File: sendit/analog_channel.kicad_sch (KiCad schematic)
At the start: 6 parts

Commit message: bigger update
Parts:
- added C5: 100nF, Capacitor_SMD:C_0805_2012Metric_Pad1.18x1.45mm_HandSolder, symbol Device:C_Small
- added F1: 30v / 30mA, Fuse:Fuse_0603_1608Metric, symbol Device:Polyfuse_Small
- added R13: 1.5K 0.1%, Resistor_SMD:R_1206_3216Metric_Pad1.30x1.75mm_HandSolder, symbol Device:R_Small_US
- added R16: 910 0.1%, Resistor_SMD:R_1206_3216Metric_Pad1.30x1.75mm_HandSolder, symbol Device:R_Small_US
- added R2: 470 0.1%, Resistor_SMD:R_1206_3216Metric_Pad1.30x1.75mm_HandSolder, symbol Device:R_Small_US
- added R20: 1k 0.1%, Resistor_SMD:R_1206_3216Metric_Pad1.30x1.75mm_HandSolder, symbol Device:R_Small_US
- added R70: 165 0.1%, Resistor_SMD:R_1206_3216Metric_Pad1.30x1.75mm_HandSolder, symbol Device:R_Small_US
- added R8: 13K 0.1%, Resistor_SMD:R_1206_3216Metric_Pad1.30x1.75mm_HandSolder, symbol Device:R_Small_US
- added TP1, TP9: TestPoint, TestPoint:TestPoint_Pad_D1.0mm, symbol Connector:TestPoint
- added TP81: TestPoint, symbol Connector:TestPoint
- added U3: TMUX4052PWR, yarrboard:TSSOP16-PW_TEX, symbol yarrboard:TMUX4052PWR
- renumbered C11 to C1, D4 to D1, INPUT4 to INPUT1, J4 to J1, R19 to R1
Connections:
- net +24V: now also C5.1, U3.16 (VDD)
- net +3.3V: now also R20.2
- net A0: now also U3.10 (A0)
- net A1: now also U3.9 (A1)
- net EN: now also U3.6 (*EN)
- net GND: now also C5.2, R13.1, R16.1, R70.1, U3.7 (VSS), U3.8 (GND)
- net OUTPUT: now also TP81.1
- net at J1.1 (Pin_1), J1.3 (Pin_3), J1.5 (Pin_5): now also F1.1; no longer INPUT1.1 (Pin_1)
- net ADC MUX - TMUX4052/DA: no longer names the net of D9.3 (COM), INPUT1.2 (Pin_2)
- net ADC MUX - TMUX4052/DA: now also TP1.1, U3.13 (DA)
- net ADC MUX - TMUX4052/DB: no longer names the net of R1.1
- net ADC MUX - TMUX4052/DB: now also TP9.1, U3.3 (DB)
- new net: R20.1, U3.15 (S2A), U3.2 (S2B)
- new net: F1.2, INPUT1.1 (Pin_1)
- new net: R13.2, R8.1, U3.5 (S1B)
- new net: R16.2, R2.1, U3.4 (S3B)
- new net: R8.2, U3.14 (S1A)
- new net: R70.2, U3.1 (S0B), U3.12 (S0A)
- new net: R2.2, U3.11 (S3A)
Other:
- removed sheet 0-1000 ohm
- removed sheet 0-32v
- removed sheet 0-5v
- removed sheet 4-20mA
- removed sheet ADC MUX - TMUX4052
- note added: "(resistor wired from input to ground)"
- note added: "0-1000 ohm Resistance Sensor"
- note added: "32v to 3.3v Voltage Divider"
- note added: "4-20ma Current Sensor"
- note added: "5v to 3.3v Voltage Divider"
- note added: "Analog MUX - 4:1 - 2CH"
- note added: "Different Types of Input Signals:"
- note added: "Input Stage"
- note added: "Output Stage"
- moved on the sheet: C1, D1, D9, INPUT1, J1, R1

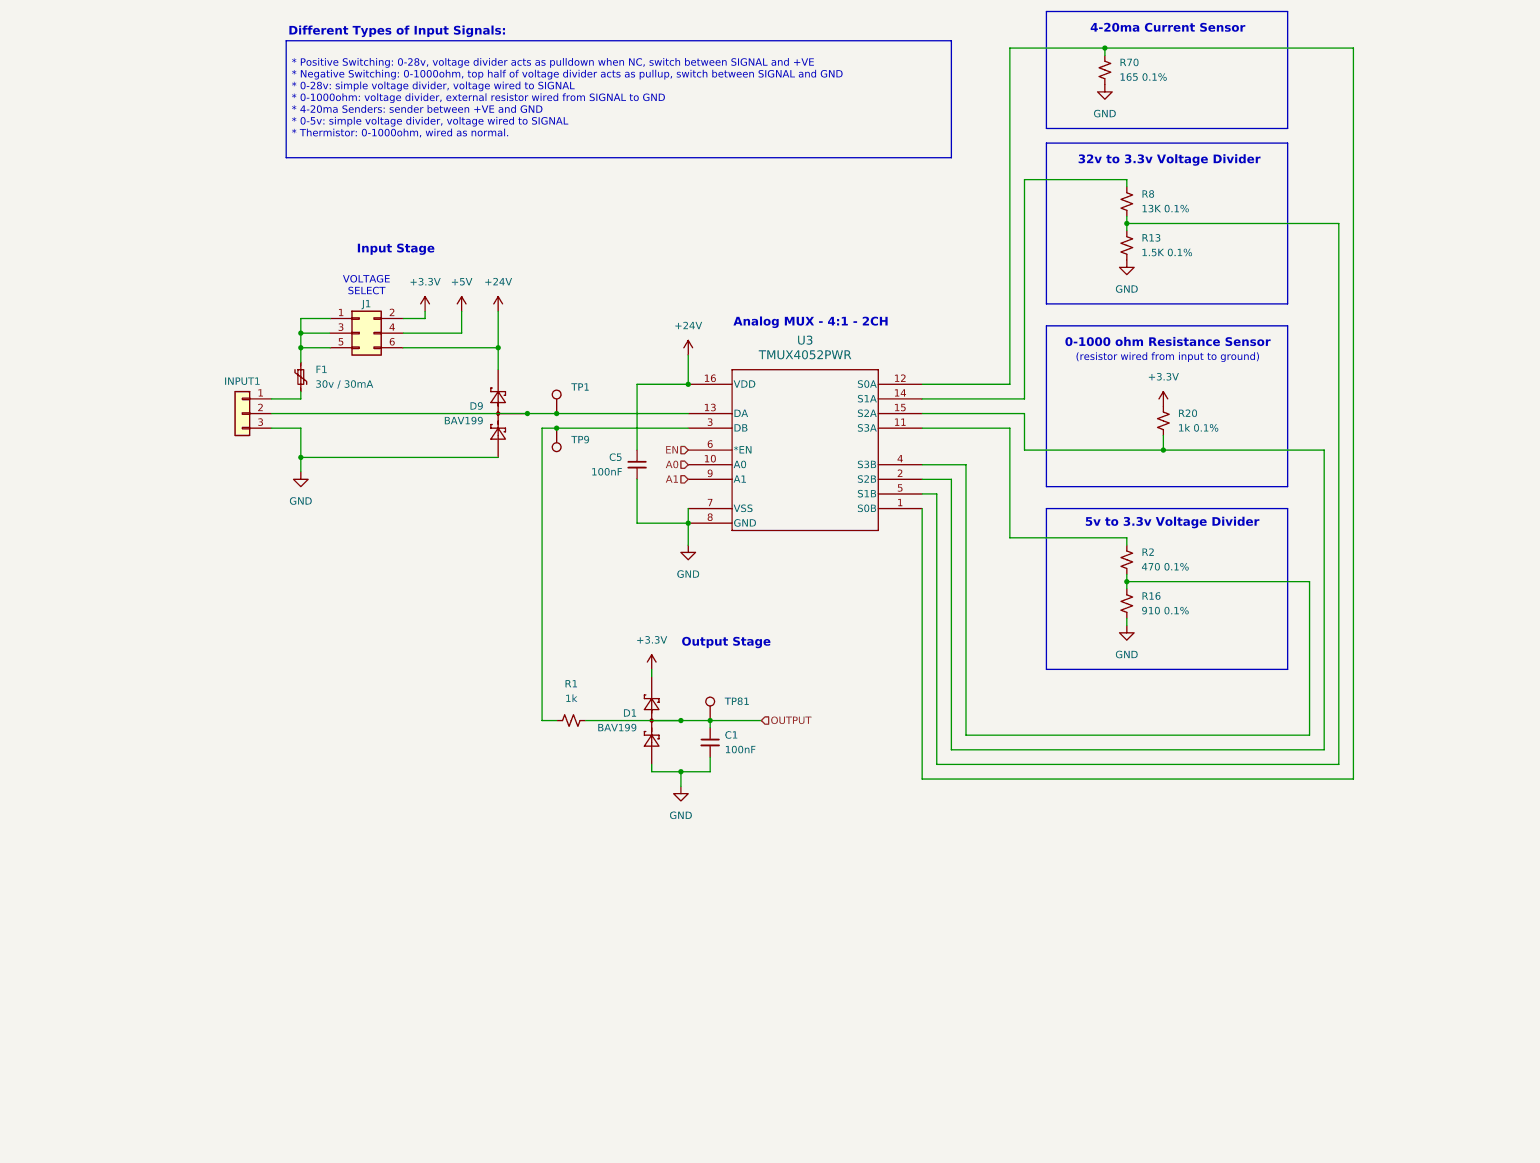
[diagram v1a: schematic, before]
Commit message: changed from mux to pin jumpers
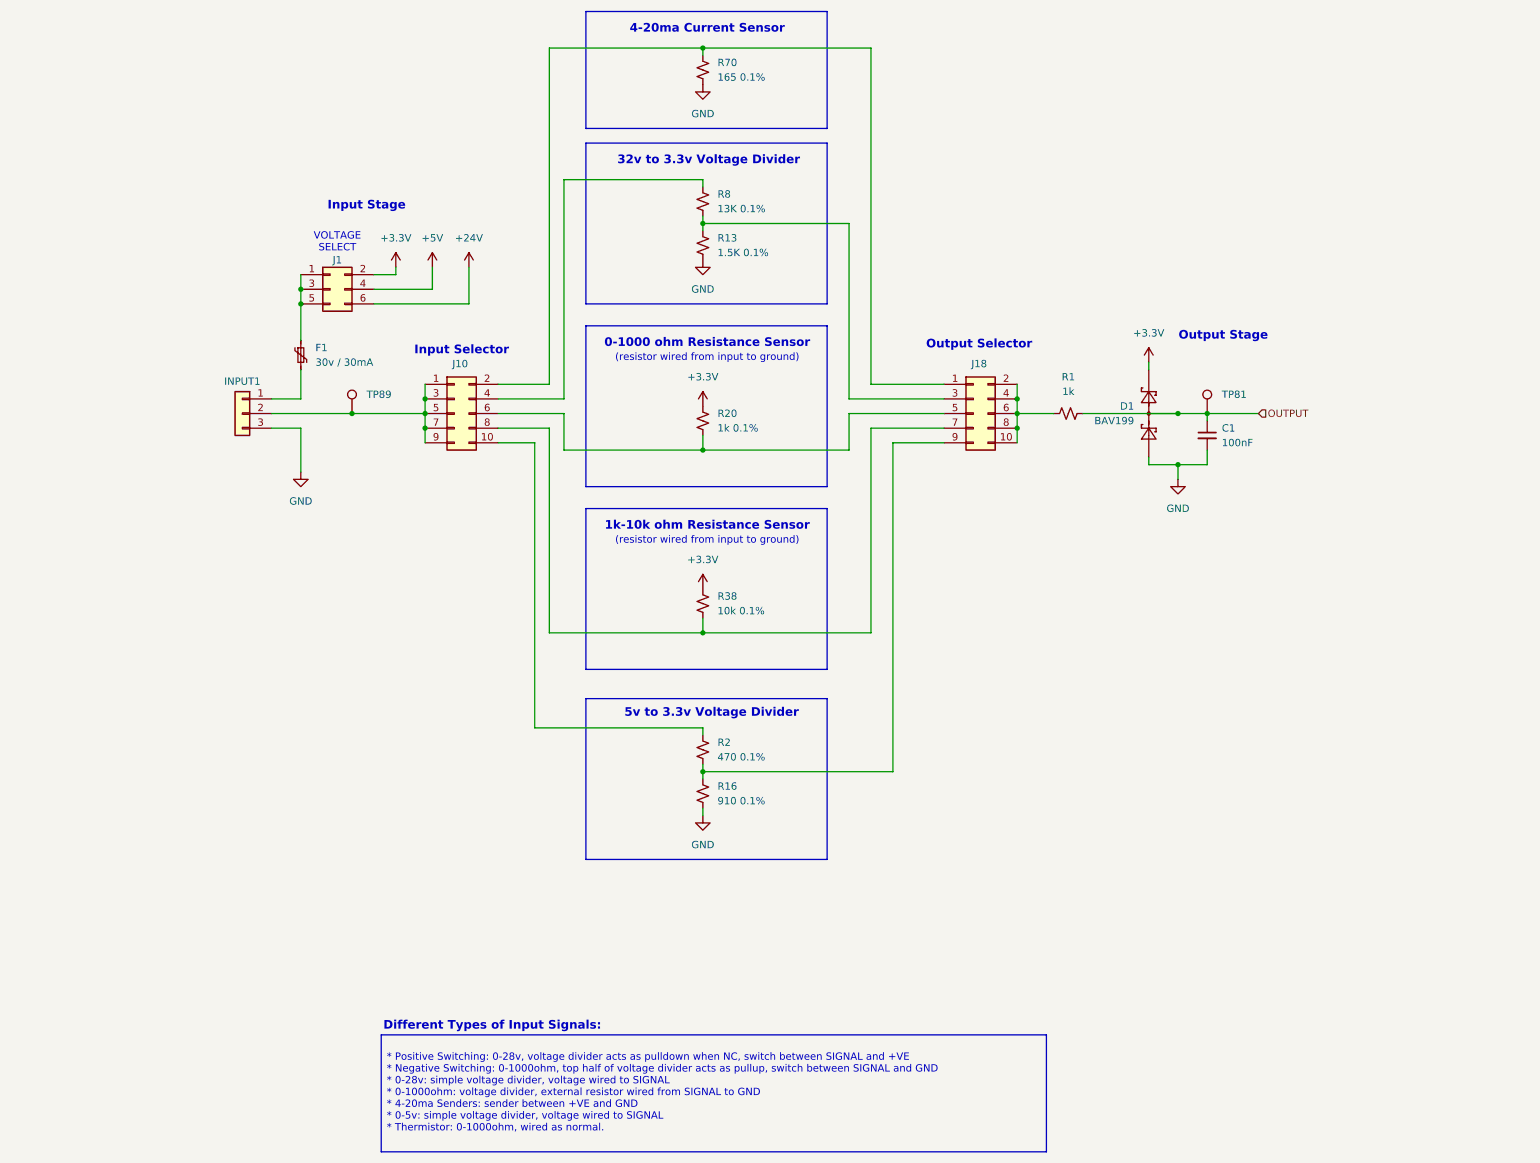
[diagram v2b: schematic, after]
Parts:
- removed C5: 100nF, Capacitor_SMD:C_0805_2012Metric_Pad1.18x1.45mm_HandSolder, symbol Device:C_Small
- removed D9: BAV199, Package_TO_SOT_SMD:SOT-23, symbol Diode:BAT54S
- removed TP1, TP9: TestPoint, TestPoint:TestPoint_Pad_D1.0mm, symbol Connector:TestPoint
- removed U3: TMUX4052PWR, yarrboard:TSSOP16-PW_TEX, symbol yarrboard:TMUX4052PWR
- added J10, J18: Conn_02x05_Odd_Even, Connector_PinHeader_2.54mm:PinHeader_2x05_P2.54mm_Vertical_SMD, symbol Connector_Generic:Conn_02x05_Odd_Even
- added R38: 10k 0.1%, Resistor_SMD:R_0603_1608Metric, symbol Device:R_Small_US
- added TP89: TestPoint, TestPoint:TestPoint_Pad_D1.0mm, symbol Connector:TestPoint
- J1: footprint Connector_PinHeader_2.54mm:PinHeader_2x03_P2.54mm_Vertical -> Connector_PinHeader_2.54mm:PinHeader_2x03_P2.54mm_Vertical_SMD
- R13, R16, R2, R20, R8: footprint Resistor_SMD:R_1206_3216Metric_Pad1.30x1.75mm_HandSolder -> Resistor_SMD:R_0603_1608Metric
- TP81: footprint (none) -> TestPoint:TestPoint_Pad_D1.0mm
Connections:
- net +3.3V: now also R38.2
- net at R20.1: now also J10.6 (Pin_6), J18.5 (Pin_5)
- net at INPUT1.2 (Pin_2): now also J10.1 (Pin_1), J10.3 (Pin_3), J10.5 (Pin_5), J10.7 (Pin_7), J10.9 (Pin_9), TP89.1
- net at R13.2, R8.1: now also J18.3 (Pin_3)
- net at R16.2, R2.1: now also J18.9 (Pin_9)
- net at R8.2: now also J10.4 (Pin_4)
- net at R70.2: now also J10.2 (Pin_2), J18.1 (Pin_1)
- net at R2.2: now also J10.10 (Pin_10)
- net at R1.1: now also J18.10 (Pin_10), J18.2 (Pin_2), J18.4 (Pin_4), J18.6 (Pin_6), J18.8 (Pin_8)
- new net: J10.8 (Pin_8), J18.7 (Pin_7), R38.1
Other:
- note added: "1k-10k ohm Resistance Sensor"
- note added: "Input Selector"
- note added: "Output Selector"
- note removed: "Analog MUX - 4:1 - 2CH"
- moved on the sheet: C1, D1, F1, J1, R1, R13, R16, R2, R20, R70, R8, TP81

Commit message: layout work.
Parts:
- renumbered J10 to J2, J18 to J3, R70 to R1, R8 to R2, R13 to R3, R20 to R4, R38 to R5, R2 to R6, R16 to R7, R1 to R8, TP89 to TP1, TP81 to TP2

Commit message: updated footprints and lcsc numbers.
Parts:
- C1: footprint Capacitor_SMD:C_0805_2012Metric_Pad1.18x1.45mm_HandSolder -> Capacitor_SMD:C_0603_1608Metric; LCSC C49678 -> C14663
- J1: LCSC (none) -> C49286562
- J2, J3: LCSC (none) -> C49286564
- R1: LCSC (none) -> C870446
- R2: LCSC (none) -> C861121
- R3: LCSC (none) -> C705741
- R4: value 1k 0.1% -> 1k 1%; LCSC (none) -> C110776
- R6: value 470 0.1% -> 560 0.1%; LCSC (none) -> C860442
- R7: value 910 0.1% -> 1k 0.1%; LCSC (none) -> C110776
- R8: footprint Resistor_SMD:R_0805_2012Metric_Pad1.20x1.40mm_HandSolder -> Resistor_SMD:R_0603_1608Metric; LCSC C95781 -> (none)
- TP1, TP2: now left out of the parts list
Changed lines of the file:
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@@
 			)
 		)
-		(property "Value" "1k 0.1%"
+		(property "Value" "1k 1%"
 			(at 140.97 92.71 0)
 			(effects
@@
 			)
 		)
-		(property "LCSC" ""
+		(property "LCSC" "C110776"
 			(at 138.43 91.44 0)
 			(effects
@@
 			)
 		)
+		(property "LCSC" "C49286564"
+			(at 95.25 90.17 0)
+			(effects
+				(font
+					(size 1.27 1.27)
+				)
+				(hide yes)
+			)
+		)
 		(pin "1"
 		)
@@
 			)
 		)
-		(property "LCSC" ""
+		(property "LCSC" "C705741"
 			(at 138.43 60.96 0)
 			(effects
@@
 			)
 		)
-		(property "Value" "910 0.1%"
+		(property "Value" "1k 0.1%"
 			(at 140.97 157.48 0)
 			(effects
@@
 			)
 		)
-		(property "LCSC" ""
+		(property "LCSC" "C110776"
 			(at 138.43 156.21 0)
 			(effects
@@
 			)
 		)
+		(property "LCSC" "C49286564"
+			(at 185.42 90.17 0)
+			(effects
+				(font
+					(size 1.27 1.27)
+				)
+				(hide yes)
+			)
+		)
 		(pin "1"
 		)
@@
 			)
 		)
-		(property "LCSC" ""
+		(property "LCSC" "C861121"
 			(at 138.43 53.34 0)
 			(effects
@@
 			)
 		)
-		(property "LCSC" ""
+		(property "LCSC" "C870446"
 			(at 138.43 30.48 0)
 			(effects
@@
 			)
 		)
-		(property "Value" "470 0.1%"
+		(property "Value" "560 0.1%"
 			(at 140.97 149.8599 0)
 			(effects
@@
 			)
 		)
-		(property "LCSC" ""
+		(property "LCSC" "C860442"
 			(at 138.43 148.59 0)
 			(effects
@@
 			)
 		)
-		(property "Footprint" "Resistor_SMD:R_0805_2012Metric_Pad1.20x1.40mm_HandSolder"
+		(property "Footprint" "Resistor_SMD:R_0603_1608Metric"
 			(at 201.93 90.17 0)
 			(effects
@@
 			)
 		)
-		(property "LCSC" "C95781"
+		(property "LCSC" ""
 			(at 201.93 90.17 0)
 			(effects
@@
 		(unit 1)
 		(exclude_from_sim no)
-		(in_bom yes)
+		(in_bom no)
 		(on_board yes)
 		(dnp no)
@@
 			)
 		)
-		(property "Footprint" "Capacitor_SMD:C_0805_2012Metric_Pad1.18x1.45mm_HandSolder"
+		(property "Footprint" "Capacitor_SMD:C_0603_1608Metric"
 			(at 226.06 93.98 0)
 			(effects
@@
 			)
 		)
-		(property "LCSC" "C49678"
+		(property "LCSC" "C14663"
 			(at 226.06 93.98 0)
 			(effects
@@
 			)
 		)
+		(property "LCSC" "C49286562"
+			(at 73.66 68.58 0)
+			(effects
+				(font
+					(size 1.27 1.27)
+				)
+				(hide yes)
+			)
+		)
 		(pin "5"
 		)
@@
 		(unit 1)
 		(exclude_from_sim no)
-		(in_bom yes)
+		(in_bom no)
 		(on_board yes)
 		(dnp no)

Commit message: added fuses, 24v filters, and indicator leds.
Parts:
- J1: footprint Connector_PinHeader_2.54mm:PinHeader_2x03_P2.54mm_Vertical_SMD -> Connector_PinHeader_2.54mm:PinHeader_2x03_P2.54mm_Vertical; LCSC C49286562 -> C32713283
- J2, J3: footprint Connector_PinHeader_2.54mm:PinHeader_2x05_P2.54mm_Vertical_SMD -> Connector_PinHeader_2.54mm:PinHeader_2x05_P2.54mm_Vertical; LCSC C49286564 -> C32713285
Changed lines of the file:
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@@
 			)
 		)
-		(property "Footprint" "Connector_PinHeader_2.54mm:PinHeader_2x05_P2.54mm_Vertical_SMD"
+		(property "Footprint" "Connector_PinHeader_2.54mm:PinHeader_2x05_P2.54mm_Vertical"
 			(at 95.25 90.17 0)
 			(effects
@@
 			)
 		)
-		(property "LCSC" "C49286564"
+		(property "LCSC" "C32713285"
 			(at 95.25 90.17 0)
 			(effects
@@
 			)
 		)
-		(property "Footprint" "Connector_PinHeader_2.54mm:PinHeader_2x05_P2.54mm_Vertical_SMD"
+		(property "Footprint" "Connector_PinHeader_2.54mm:PinHeader_2x05_P2.54mm_Vertical"
 			(at 185.42 90.17 0)
 			(effects
@@
 			)
 		)
-		(property "LCSC" "C49286564"
+		(property "LCSC" "C32713285"
 			(at 185.42 90.17 0)
 			(effects
@@
 			)
 		)
-		(property "Footprint" "Connector_PinHeader_2.54mm:PinHeader_2x03_P2.54mm_Vertical_SMD"
+		(property "Footprint" "Connector_PinHeader_2.54mm:PinHeader_2x03_P2.54mm_Vertical"
 			(at 73.66 68.58 0)
 			(effects
@@
 			)
 		)
-		(property "LCSC" "C49286562"
+		(property "LCSC" "C32713283"
 			(at 73.66 68.58 0)
 			(effects

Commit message: test run of jlcpcb upload looks good.
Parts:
- added J26: Conn_01x03, symbol Connector_Generic:Conn_01x03
- C1: value 100nF -> 100nF / 50v
- D1: LCSC C549304 -> C40919; Mouser 637-BAV199 -> (none)
- F1: value 30v / 30mA -> 30mA / 30v
- INPUT1: LCSC C5188296 and C5188250 -> C5188296
- J1: LCSC C32713283 -> C225518
- J2, J3: LCSC C32713285 -> C225520
- R1: footprint Resistor_SMD:R_1206_3216Metric_Pad1.30x1.75mm_HandSolder -> Resistor_SMD:R_1206_3216Metric
- R4: value 1k 1% -> 1k 0.1%
- R5: LCSC (none) -> C95204
- R8: LCSC (none) -> C21190
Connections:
- no-connect marks 0 -> 3
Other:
- note added: "Different Types of Usage:"
- note added: "FEMALE"
- note added: "MALE"
- note removed: "Different Types of Input Signals:"
- moved on the sheet: C1, D1, F1, INPUT1, J1, J2, J3, R1, R2, R3, R4, R5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

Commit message: fully routed again.
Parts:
- TP2: footprint TestPoint:TestPoint_Pad_D1.0mm -> TestPoint:TestPoint_THTPad_D1.0mm_Drill0.5mm
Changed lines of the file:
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@@
 			)
 		)
-		(property "Footprint" "TestPoint:TestPoint_Pad_D1.0mm"
+		(property "Footprint" "TestPoint:TestPoint_THTPad_D1.0mm_Drill0.5mm"
 			(at 210.82 101.6 0)
 			(effects

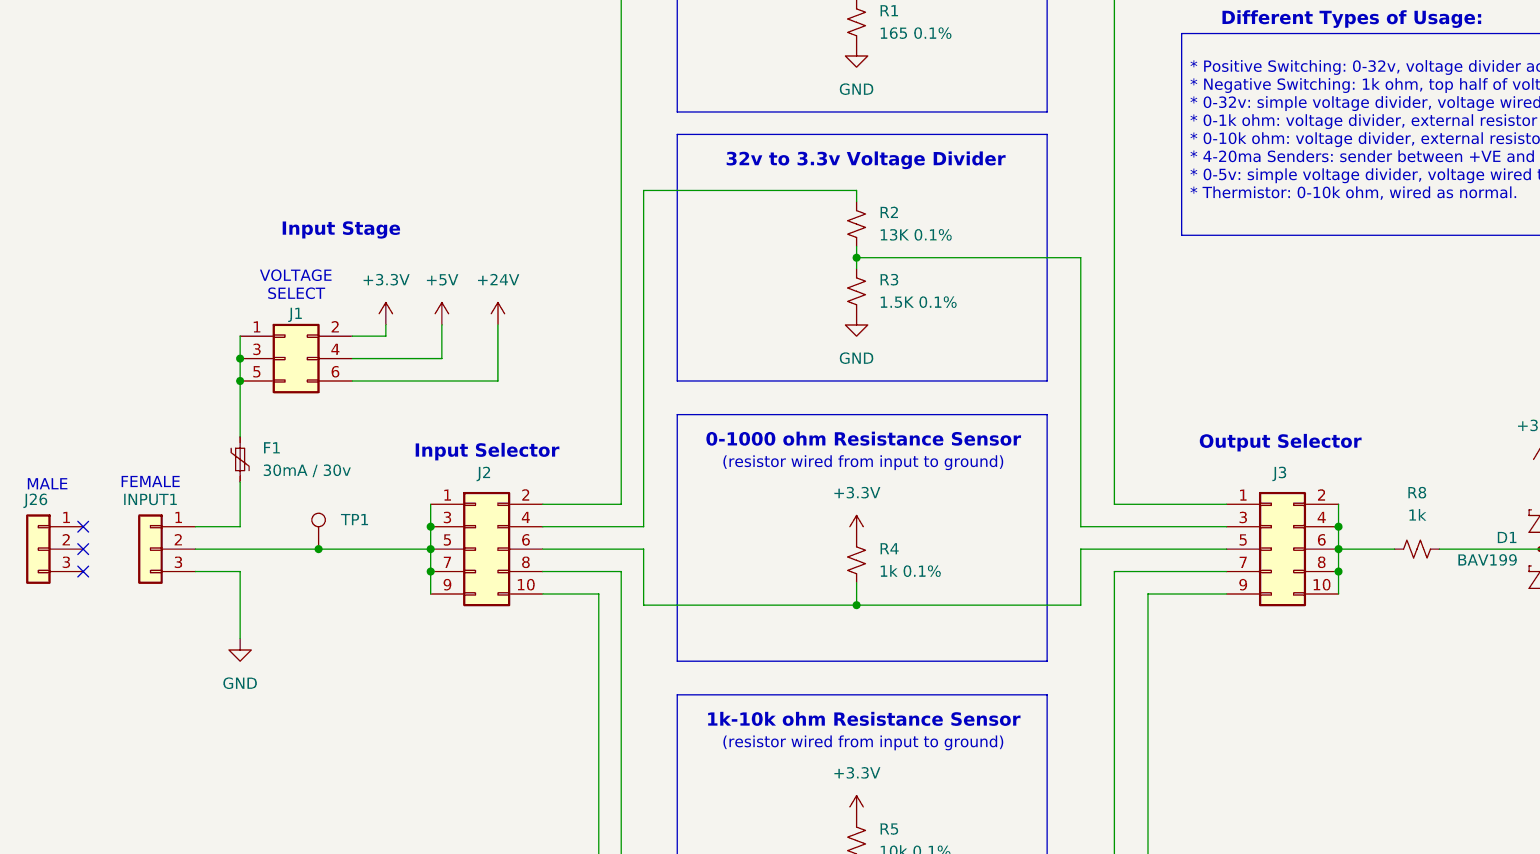
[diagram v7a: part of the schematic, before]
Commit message: added shunts to the BOM
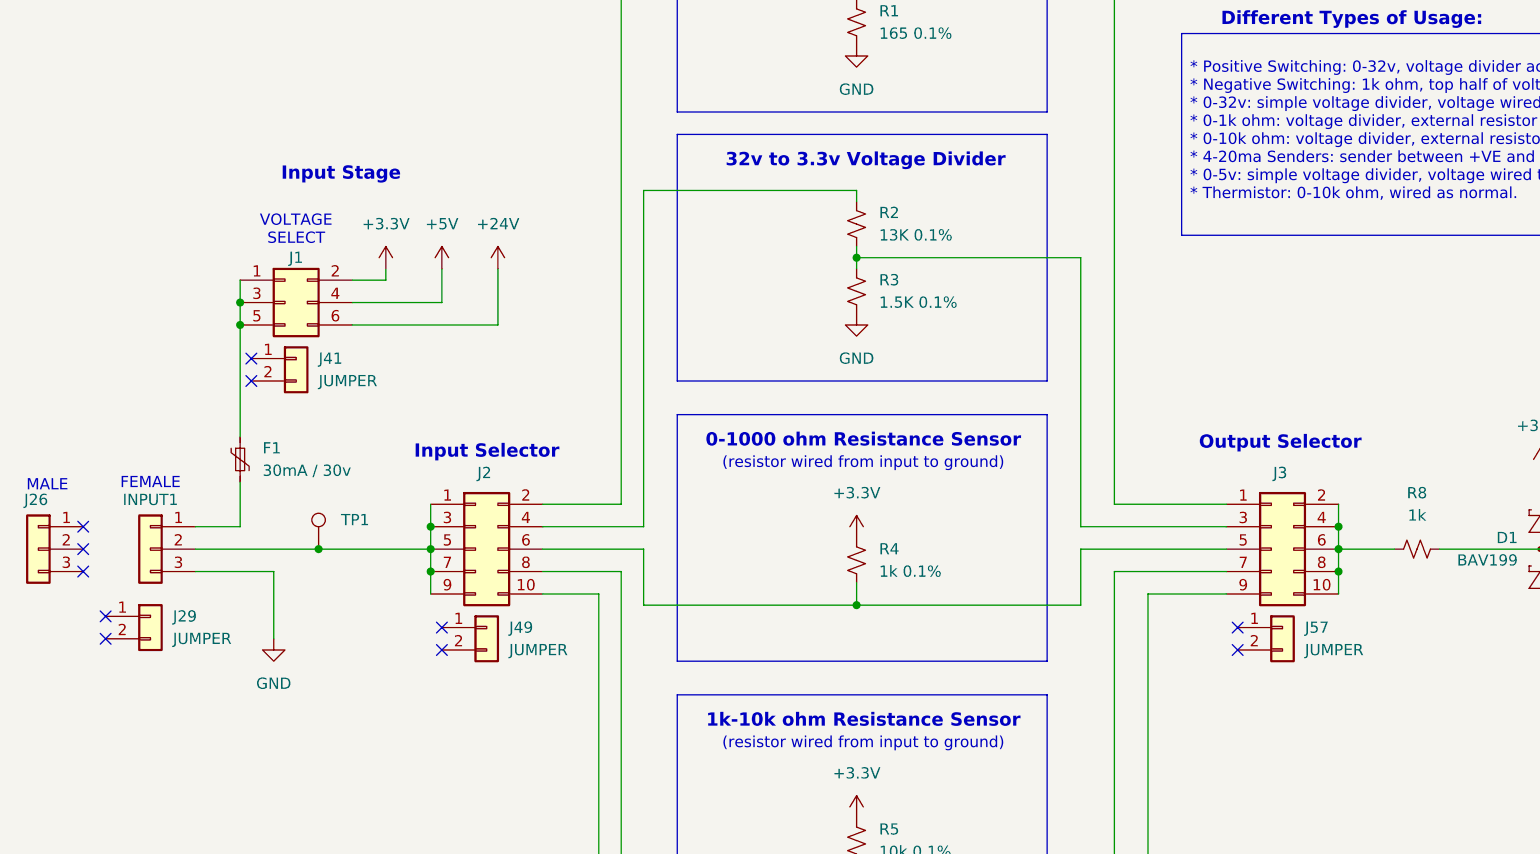
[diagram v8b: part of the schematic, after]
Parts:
- added J29, J41, J49, J57: JUMPER, symbol Connector_Generic:Conn_01x02
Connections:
- no-connect marks 3 -> 11
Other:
- moved on the sheet: J1
